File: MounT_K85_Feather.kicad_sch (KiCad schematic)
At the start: 10 parts, among them J1 Adafruit_Feather, J2 DB25_Male, SW1 CUS-12TB, U1 MAX3232

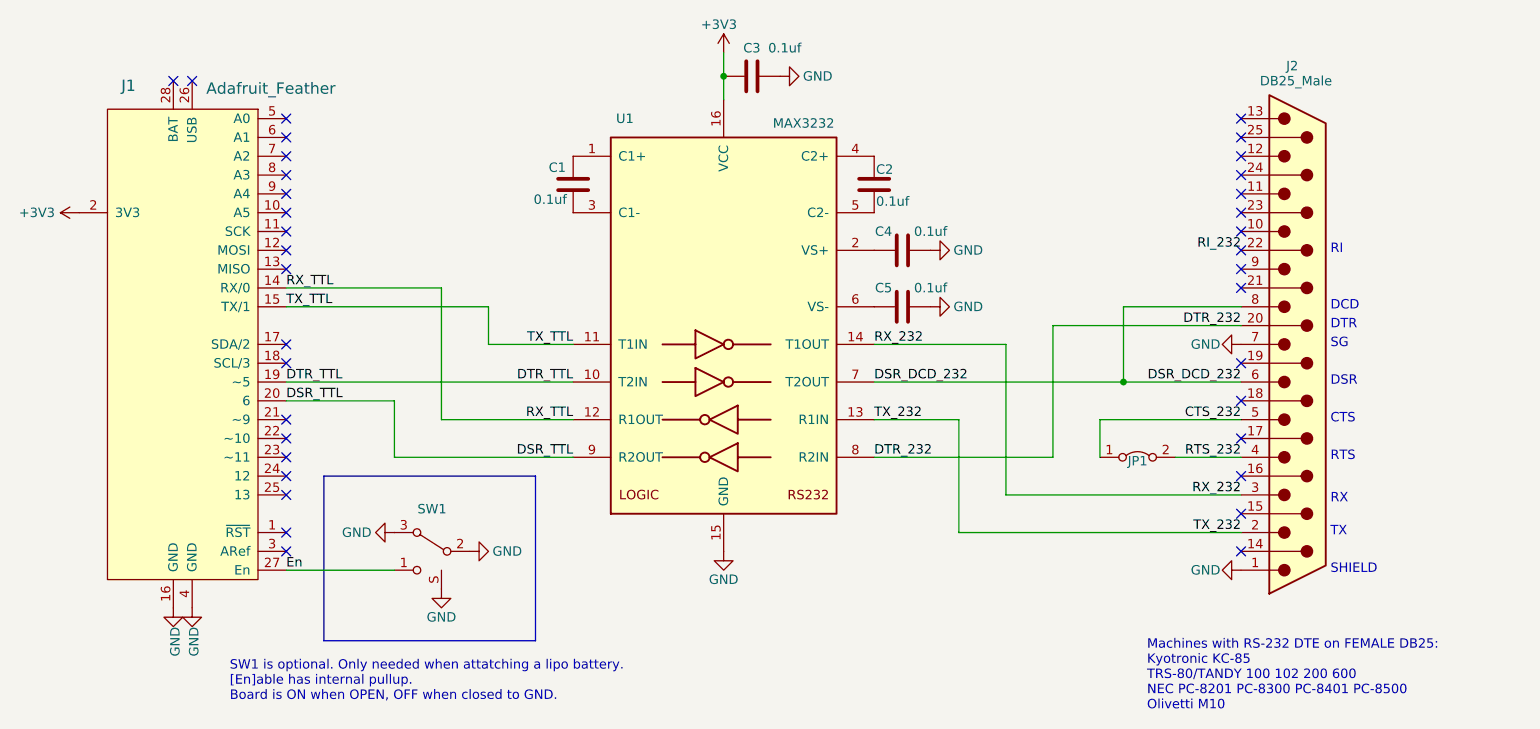
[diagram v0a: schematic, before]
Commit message: smt power switch on feather, routing 3v3 on teensy, silkscreen all
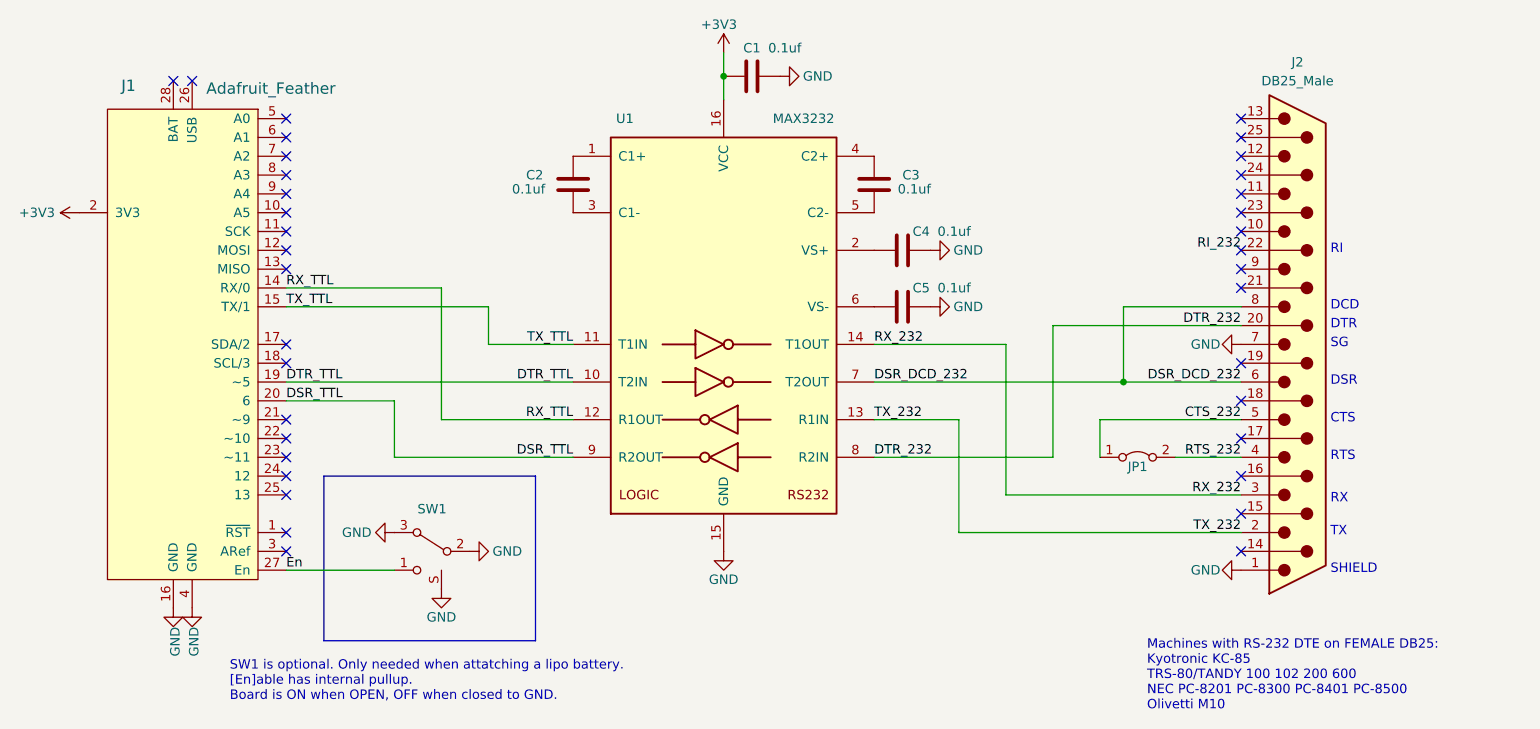
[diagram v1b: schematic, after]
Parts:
- renumbered C3 to C1, C1 to C2, C2 to C3
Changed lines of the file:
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@@
+    (stroke (width 0) (type default) (color 0 0 0 0))
+  )
+  (wire (pts (xy 160.02 118.11) (xy 184.15 118.11))
+    (stroke (width 0) (type default) (color 0 0 0 0))
+  )
+  (wire (pts (xy 177.8 102.87) (xy 177.8 123.19))
+    (stroke (width 0) (type default) (color 0 0 0 0))
+  )
+  (wire (pts (xy 95.25 110.49) (xy 95.25 118.11))
+    (stroke (width 0) (type default) (color 0 0 0 0))
+  )
+  (wire (pts (xy 80.645 107.95) (xy 119.38 107.95))
+    (stroke (width 0) (type default) (color 0 0 0 0))
+  )
+  (wire (pts (xy 184.15 118.11) (xy 184.15 100.33))
+    (stroke (width 0) (type default) (color 0 0 0 0))
+  )
+  (polyline (pts (xy 85.725 120.65) (xy 85.725 142.875))
+    (stroke (width 0) (type default) (color 0 0 0 0))
+  )
+  (wire (pts (xy 193.675 97.79) (xy 209.55 97.79))
+    (stroke (width 0) (type default) (color 0 0 0 0))
+  )
+  (wire (pts (xy 171.45 128.27) (xy 209.55 128.27))
+    (stroke (width 0) (type default) (color 0 0 0 0))
+  )
+  (wire (pts (xy 107.95 97.79) (xy 107.95 102.87))
+    (stroke (width 0) (type default) (color 0 0 0 0))
+  )
+  (wire (pts (xy 80.645 95.25) (xy 101.6 95.25))
+    (stroke (width 0) (type default) (color 0 0 0 0))
+  )
+  (polyline (pts (xy 85.725 142.875) (xy 114.3 142.875))
+    (stroke (width 0) (type default) (color 0 0 0 0))
+  )
+  (wire (pts (xy 80.645 97.79) (xy 107.95 97.79))
+    (stroke (width 0) (type default) (color 0 0 0 0))
+  )
+  (wire (pts (xy 107.95 102.87) (xy 119.38 102.87))
+    (stroke (width 0) (type default) (color 0 0 0 0))
+  )
+  (wire (pts (xy 171.45 113.03) (xy 171.45 128.27))
+    (stroke (width 0) (type default) (color 0 0 0 0))
+  )
+  (wire (pts (xy 101.6 113.03) (xy 119.38 113.03))
+    (stroke (width 0) (type default) (color 0 0 0 0))
+  )
+  (wire (pts (xy 160.02 102.87) (xy 177.8 102.87))
+    (stroke (width 0) (type default) (color 0 0 0 0))
+  )
+  (wire (pts (xy 193.675 107.95) (xy 193.675 97.79))
+    (stroke (width 0) (type default) (color 0 0 0 0))
+  )
+  (wire (pts (xy 193.675 107.95) (xy 209.55 107.95))
+    (stroke (width 0) (type default) (color 0 0 0 0))
+  )
+  (wire (pts (xy 190.5 118.11) (xy 190.5 113.03))
+    (stroke (width 0) (type default) (color 0 0 0 0))
+  )
+  (wire (pts (xy 80.645 110.49) (xy 95.25 110.49))
     (stroke (width 0) (type default) (color 0 0 0 0))
   )
   (wire (pts (xy 160.02 107.95) (xy 193.675 107.95))
-    (stroke (width 0) (type default) (color 0 0 0 0))
-  )
-  (wire (pts (xy 193.675 107.95) (xy 209.55 107.95))
-    (stroke (width 0) (type default) (color 0 0 0 0))
-  )
-  (wire (pts (xy 160.02 118.11) (xy 184.15 118.11))
-    (stroke (width 0) (type default) (color 0 0 0 0))
-  )
-  (wire (pts (xy 177.8 102.87) (xy 177.8 123.19))
-    (stroke (width 0) (type default) (color 0 0 0 0))
-  )
-  (wire (pts (xy 95.25 110.49) (xy 95.25 118.11))
-    (stroke (width 0) (type default) (color 0 0 0 0))
-  )
-  (wire (pts (xy 80.645 107.95) (xy 119.38 107.95))
-    (stroke (width 0) (type default) (color 0 0 0 0))
-  )
-  (wire (pts (xy 184.15 118.11) (xy 184.15 100.33))
-    (stroke (width 0) (type default) (color 0 0 0 0))
-  )
-  (polyline (pts (xy 85.725 120.65) (xy 85.725 142.875))
-    (stroke (width 0) (type default) (color 0 0 0 0))
-  )
-  (wire (pts (xy 193.675 97.79) (xy 209.55 97.79))
-    (stroke (width 0) (type default) (color 0 0 0 0))
-  )
-  (wire (pts (xy 171.45 128.27) (xy 209.55 128.27))
-    (stroke (width 0) (type default) (color 0 0 0 0))
-  )
-  (wire (pts (xy 107.95 97.79) (xy 107.95 102.87))
-    (stroke (width 0) (type default) (color 0 0 0 0))
-  )
-  (wire (pts (xy 80.645 95.25) (xy 101.6 95.25))
-    (stroke (width 0) (type default) (color 0 0 0 0))
-  )
-  (polyline (pts (xy 85.725 142.875) (xy 114.3 142.875))
-    (stroke (width 0) (type default) (color 0 0 0 0))
-  )
-  (wire (pts (xy 80.645 97.79) (xy 107.95 97.79))
-    (stroke (width 0) (type default) (color 0 0 0 0))
-  )
-  (wire (pts (xy 107.95 102.87) (xy 119.38 102.87))
-    (stroke (width 0) (type default) (color 0 0 0 0))
-  )
-  (wire (pts (xy 171.45 113.03) (xy 171.45 128.27))
-    (stroke (width 0) (type default) (color 0 0 0 0))
-  )
-  (wire (pts (xy 101.6 113.03) (xy 119.38 113.03))
-    (stroke (width 0) (type default) (color 0 0 0 0))
-  )
-  (wire (pts (xy 160.02 102.87) (xy 177.8 102.87))
-    (stroke (width 0) (type default) (color 0 0 0 0))
-  )
-  (wire (pts (xy 193.675 107.95) (xy 193.675 97.79))
-    (stroke (width 0) (type default) (color 0 0 0 0))
-  )
-  (wire (pts (xy 190.5 118.11) (xy 190.5 113.03))
-    (stroke (width 0) (type default) (color 0 0 0 0))
-  )
-  (wire (pts (xy 80.645 110.49) (xy 95.25 110.49))
     (stroke (width 0) (type default) (color 0 0 0 0))
   )
@@
   (symbol (lib_id "0_LOCAL:DB25_Male") (at 217.17 102.87 0) (unit 1)
     (in_bom yes) (on_board yes)
-    (property "Reference" "J2" (id 0) (at 215.646 65.278 0)
-      (effects (font (size 1.27 1.27)) (justify left))
-    )
-    (property "Value" "DB25_Male" (id 1) (at 212.09 67.31 0)
-      (effects (font (size 1.27 1.27)) (justify left))
-    )
+    (property "Reference" "J2" (id 0) (at 217.17 64.77 0))
+    (property "Value" "DB25_Male" (id 1) (at 217.17 67.31 0))
     (property "Footprint" "0_LOCAL:DSUB-25_Male_Vertical_P2.77x2.84mm" (id 2) (at 217.17 102.87 0)
       (effects (font (size 1.27 1.27)) hide)
@@
   (symbol (lib_id "0_LOCAL:Jumper_2_Bridged") (at 195.58 118.11 0) (unit 1)
     (in_bom yes) (on_board yes)
-    (property "Reference" "JP1" (id 0) (at 195.58 118.618 0))
+    (property "Reference" "JP1" (id 0) (at 195.58 119.38 0))
     (property "Value" "Jumper_2_Bridged" (id 1) (at 196.342 115.316 0)
       (effects (font (size 1.27 1.27)) hide)
@@
     (in_bom yes) (on_board yes)
     (property "Reference" "U1" (id 0) (at 126.365 72.39 0))
-    (property "Value" "MAX3232" (id 1) (at 150.495 73.025 0))
+    (property "Value" "MAX3232" (id 1) (at 150.495 72.39 0))
     (property "Footprint" "0_LOCAL:SOIC-16_W3.90mm" (id 2) (at 140.97 127 0)
       (effects (font (size 1.27 1.27)) (justify left) hide)
@@
   (symbol (lib_id "0_LOCAL:C") (at 160.02 81.28 0) (unit 1)
     (in_bom yes) (on_board yes)
-    (property "Reference" "C2" (id 0) (at 160.274 79.248 0)
+    (property "Reference" "C3" (id 0) (at 163.83 80.01 0)
       (effects (font (size 1.27 1.27)) (justify left))
     )
-    (property "Value" "0.1uf" (id 1) (at 160.274 83.566 0)
+    (property "Value" "0.1uf" (id 1) (at 163.195 81.915 0)
       (effects (font (size 1.27 1.27)) (justify left))
     )
@@
   (symbol (lib_id "0_LOCAL:C") (at 119.38 81.28 0) (unit 1)
     (in_bom yes) (on_board yes)
-    (property "Reference" "C1" (id 0) (at 116.078 78.994 0)
+    (property "Reference" "C2" (id 0) (at 113.03 80.01 0)
       (effects (font (size 1.27 1.27)) (justify left))
     )
-    (property "Value" "0.1uf" (id 1) (at 114.046 83.312 0)
+    (property "Value" "0.1uf" (id 1) (at 111.125 81.915 0)
       (effects (font (size 1.27 1.27)) (justify left))
     )
@@
   (symbol (lib_id "0_LOCAL:C") (at 163.83 90.17 90) (unit 1)
     (in_bom yes) (on_board yes)
-    (property "Reference" "C4" (id 0) (at 161.29 87.63 90))
-    (property "Value" "0.1uf" (id 1) (at 167.64 87.63 90))
+    (property "Reference" "C4" (id 0) (at 166.37 87.63 90))
+    (property "Value" "0.1uf" (id 1) (at 170.815 87.63 90))
     (property "Footprint" "0_LOCAL:C_0805" (id 2) (at 167.64 89.2048 0)
       (effects (font (size 1.27 1.27)) hide)
@@
   (symbol (lib_id "0_LOCAL:C") (at 163.83 97.79 90) (unit 1)
     (in_bom yes) (on_board yes)
-    (property "Reference" "C5" (id 0) (at 161.29 95.25 90))
-    (property "Value" "0.1uf" (id 1) (at 167.64 95.25 90))
+    (property "Reference" "C5" (id 0) (at 166.37 95.25 90))
+    (property "Value" "0.1uf" (id 1) (at 170.815 95.25 90))
     (property "Footprint" "0_LOCAL:C_0805" (id 2) (at 167.64 96.8248 0)
       (effects (font (size 1.27 1.27)) hide)
@@
   (symbol (lib_id "0_LOCAL:C") (at 143.51 66.675 90) (unit 1)
     (in_bom yes) (on_board yes)
-    (property "Reference" "C3" (id 0) (at 143.51 62.865 90))
+    (property "Reference" "C1" (id 0) (at 143.51 62.865 90))
     (property "Value" "0.1uf" (id 1) (at 147.955 62.865 90))
     (property "Footprint" "0_LOCAL:C_0805" (id 2) (at 147.32 65.7098 0)
@@
       (reference "#PWR0109") (unit 1) (value "GND") (footprint "")
     )
+    (path "/00000000-0000-0000-0000-00005f488f0f"
+      (reference "C1") (unit 1) (value "0.1uf") (footprint "0_LOCAL:C_0805")
+    )
     (path "/00000000-0000-0000-0000-00005f479cc5"
-      (reference "C1") (unit 1) (value "0.1uf") (footprint "0_LOCAL:C_0805")
+      (reference "C2") (unit 1) (value "0.1uf") (footprint "0_LOCAL:C_0805")
     )
     (path "/00000000-0000-0000-0000-00005f473fc0"
-      (reference "C2") (unit 1) (value "0.1uf") (footprint "0_LOCAL:C_0805")
-    )
-    (path "/00000000-0000-0000-0000-00005f488f0f"
       (reference "C3") (unit 1) (value "0.1uf") (footprint "0_LOCAL:C_0805")
     )
